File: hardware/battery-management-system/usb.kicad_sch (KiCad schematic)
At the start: 20 parts, among them J12 AMPHENOL_micro_usb_10118194-0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, U5 FT230XS

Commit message: fix design errors
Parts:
- renumbered D17 to D15, D18 to D16, J12 to J11, R17 to R15, R18 to R16, R19 to R17, R20 to R18, R21 to R19, R22 to R20, R23 to R21, R24 to R22

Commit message: fix design errors
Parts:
- renumbered D15 to D13, D16 to D14, J11 to J6
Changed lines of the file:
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@@
   (symbol (lib_id "benediktibk:LED_red_0603") (at 218.44 76.2 90) (unit 1)
     (in_bom yes) (on_board yes) (dnp no) (fields_autoplaced)
-    (property "Reference" "D16" (at 224.79 77.186 90)
+    (property "Reference" "D14" (at 224.79 77.186 90)
       (effects (font (size 1.27 1.27)) (justify right))
     )
@@
       (project "battery-management-system"
         (path "/5272f0ff-3069-41a9-bca2-80beede8b4b2/afdb149d-bd78-484c-a496-c5b66260efca"
-          (reference "D16") (unit 1)
+          (reference "D14") (unit 1)
         )
       )
@@
   (symbol (lib_id "benediktibk:LED_green_0603") (at 201.93 76.2 90) (unit 1)
     (in_bom yes) (on_board yes) (dnp no) (fields_autoplaced)
-    (property "Reference" "D15" (at 208.28 77.7454 90)
+    (property "Reference" "D13" (at 208.28 77.7454 90)
       (effects (font (size 1.27 1.27)) (justify right))
     )
@@
       (project "battery-management-system"
         (path "/5272f0ff-3069-41a9-bca2-80beede8b4b2/afdb149d-bd78-484c-a496-c5b66260efca"
-          (reference "D15") (unit 1)
+          (reference "D13") (unit 1)
         )
       )
@@
   (symbol (lib_id "benediktibk:AMPHENOL_micro_usb_10118194-0001LF") (at 125.73 45.72 0) (unit 1)
     (in_bom yes) (on_board yes) (dnp no) (fields_autoplaced)
-    (property "Reference" "J11" (at 126.619 30.48 0)
+    (property "Reference" "J6" (at 126.619 30.48 0)
       (effects (font (size 1.27 1.27)))
     )
@@
       (project "battery-management-system"
         (path "/5272f0ff-3069-41a9-bca2-80beede8b4b2/afdb149d-bd78-484c-a496-c5b66260efca"
-          (reference "J11") (unit 1)
-        )
-      )
+          (reference "J6") (unit 1)
+        )
+      )

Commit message: add heatsink and fix ERC errors
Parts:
- R21, R22: RS order number 901-3529 -> 199-5452
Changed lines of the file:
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@@
       (effects (font (size 1.27 1.27)) hide)
     )
-    (property "RS order number" "901-3529" (at 200.66 64.77 0)
+    (property "RS order number" "199-5452" (at 200.66 64.77 0)
       (effects (font (size 1.27 1.27)) hide)
     )
@@
       (effects (font (size 1.27 1.27)) hide)
     )
-    (property "RS order number" "901-3529" (at 184.15 64.77 0)
-      (effects (font (size 1.27 1.27)) hide)
-    )
+    (property "RS order number" "199-5452" (at 184.15 64.77 0)
+      (effects (font (size 1.27 1.27)) hide)
+    )

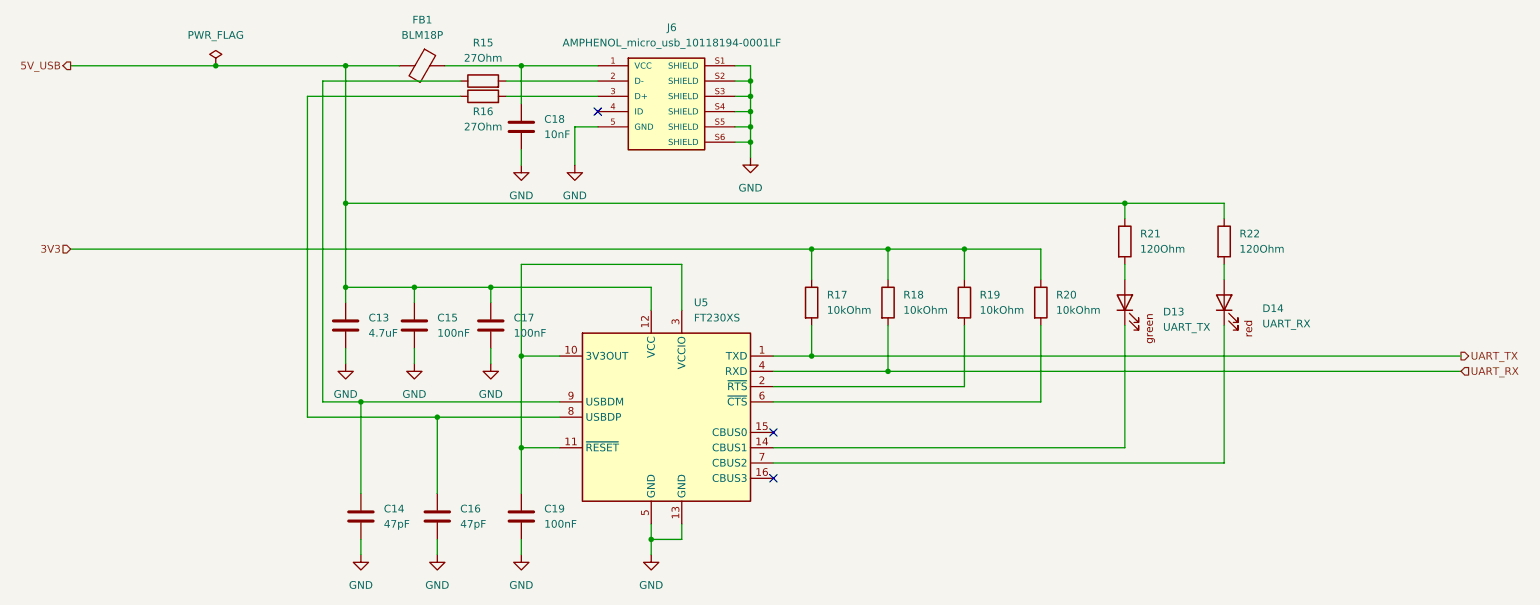
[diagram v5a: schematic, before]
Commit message: add snubber circuit
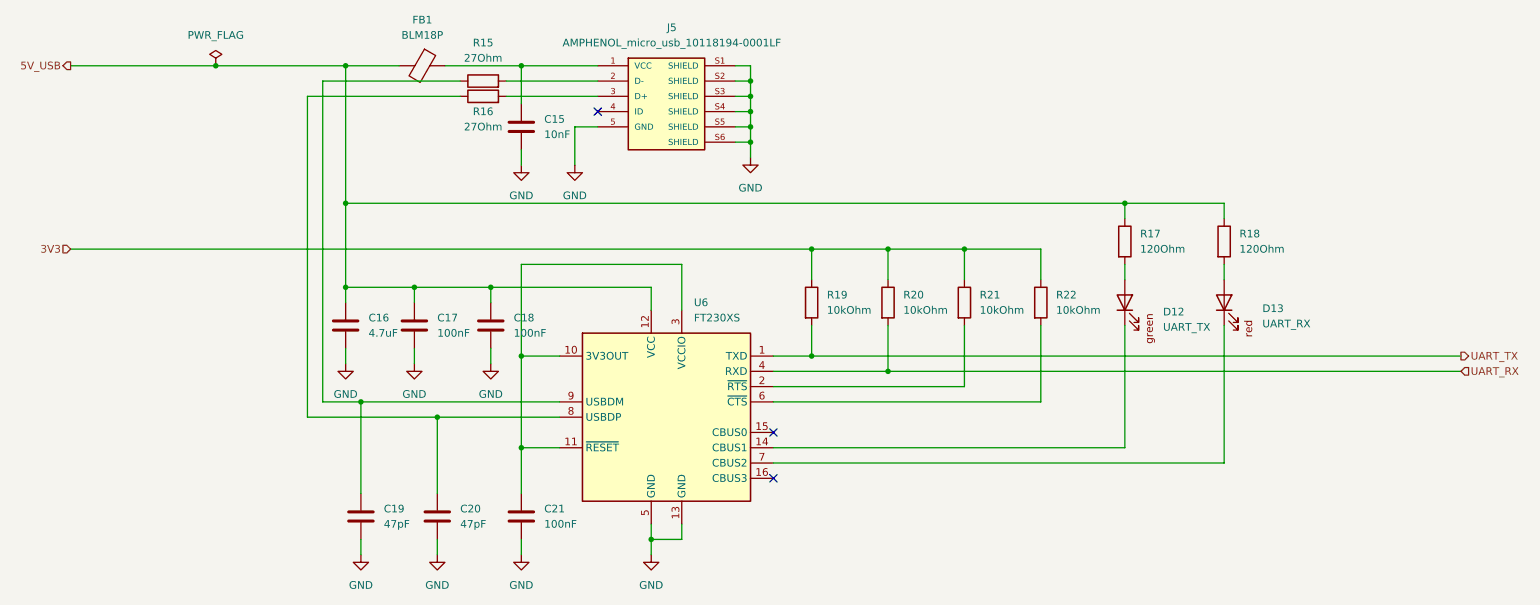
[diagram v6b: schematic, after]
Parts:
- renumbered C18 to C15, C13 to C16, C15 to C17, C17 to C18, C14 to C19, C16 to C20, C19 to C21, D13 to D12, D14 to D13, J6 to J5, R21 to R17, R22 to R18, R17 to R19, R18 to R20, R19 to R21, R20 to R22, U5 to U6
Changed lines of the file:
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@@
 		(dnp no)
 		(fields_autoplaced yes)
-		(property "Reference" "R17"
+		(property "Reference" "R19"
 			(at 152.4 74.9299 0)
 			(effects
@@
 			(project "battery-management-system"
 				(path "/5272f0ff-3069-41a9-bca2-80beede8b4b2/afdb149d-bd78-484c-a496-c5b66260efca"
-					(reference "R17")
+					(reference "R19")
 					(unit 1)
 				)
@@
 		(dnp no)
 		(fields_autoplaced yes)
-		(property "Reference" "U5"
+		(property "Reference" "U6"
 			(at 130.2894 76.2 0)
 			(effects
@@
 			(project "battery-management-system"
 				(path "/5272f0ff-3069-41a9-bca2-80beede8b4b2/afdb149d-bd78-484c-a496-c5b66260efca"
-					(reference "U5")
+					(reference "U6")
 					(unit 1)
 				)
@@
 		(dnp no)
 		(fields_autoplaced yes)
-		(property "Reference" "C19"
+		(property "Reference" "C21"
 			(at 105.41 110.4899 0)
 			(effects
@@
 			(project "battery-management-system"
 				(path "/5272f0ff-3069-41a9-bca2-80beede8b4b2/afdb149d-bd78-484c-a496-c5b66260efca"
-					(reference "C19")
+					(reference "C21")
 					(unit 1)
 				)
@@
 		(dnp no)
 		(fields_autoplaced yes)
-		(property "Reference" "#PWR035"
+		(property "Reference" "#PWR043"
 			(at 87.63 124.46 0)
 			(effects
@@
 			(project "battery-management-system"
 				(path "/5272f0ff-3069-41a9-bca2-80beede8b4b2/afdb149d-bd78-484c-a496-c5b66260efca"
-					(reference "#PWR035")
+					(reference "#PWR043")
 					(unit 1)
 				)
@@
 		(dnp no)
 		(fields_autoplaced yes)
-		(property "Reference" "#PWR034"
+		(property "Reference" "#PWR040"
 			(at 83.82 92.71 0)
 			(effects
@@
 			(project "battery-management-system"
 				(path "/5272f0ff-3069-41a9-bca2-80beede8b4b2/afdb149d-bd78-484c-a496-c5b66260efca"
-					(reference "#PWR034")
+					(reference "#PWR040")
 					(unit 1)
 				)
@@
 		(dnp no)
 		(fields_autoplaced yes)
-		(property "Reference" "D14"
+		(property "Reference" "D13"
 			(at 224.79 77.186 90)
 			(effects
@@
 			(project "battery-management-system"
 				(path "/5272f0ff-3069-41a9-bca2-80beede8b4b2/afdb149d-bd78-484c-a496-c5b66260efca"
-					(reference "D14")
+					(reference "D13")
 					(unit 1)
 				)
@@
 		(dnp no)
 		(fields_autoplaced yes)
-		(property "Reference" "C13"
+		(property "Reference" "C16"
 			(at 76.2 78.7399 0)
 			(effects
@@
 			(project "battery-management-system"
 				(path "/5272f0ff-3069-41a9-bca2-80beede8b4b2/afdb149d-bd78-484c-a496-c5b66260efca"
-					(reference "C13")
+					(reference "C16")
 					(unit 1)
 				)
@@
 		(dnp no)
 		(fields_autoplaced yes)
-		(property "Reference" "C18"
+		(property "Reference" "C15"
 			(at 105.41 45.7199 0)
 			(effects
@@
 			(project "battery-management-system"
 				(path "/5272f0ff-3069-41a9-bca2-80beede8b4b2/afdb149d-bd78-484c-a496-c5b66260efca"
-					(reference "C18")
+					(reference "C15")
 					(unit 1)
 				)
@@
 		(dnp no)
 		(fields_autoplaced yes)
-		(property "Reference" "C17"
+		(property "Reference" "C18"
 			(at 100.33 78.7399 0)
 			(effects
@@
 			(project "battery-management-system"
 				(path "/5272f0ff-3069-41a9-bca2-80beede8b4b2/afdb149d-bd78-484c-a496-c5b66260efca"
-					(reference "C17")
+					(reference "C18")
 					(unit 1)
 				)
@@
 		(dnp no)
 		(fields_autoplaced yes)
-		(property "Reference" "#PWR041"
+		(property "Reference" "#PWR036"
 			(at 139.7 58.42 0)
 			(effects
@@
 			(project "battery-management-system"
 				(path "/5272f0ff-3069-41a9-bca2-80beede8b4b2/afdb149d-bd78-484c-a496-c5b66260efca"
-					(reference "#PWR041")
+					(reference "#PWR036")
 					(unit 1)
 				)
@@
 		(dnp no)
 		(fields_autoplaced yes)
-		(property "Reference" "C15"
+		(property "Reference" "C17"
 			(at 87.63 78.7399 0)
 			(effects
@@
 			(project "battery-management-system"
 				(path "/5272f0ff-3069-41a9-bca2-80beede8b4b2/afdb149d-bd78-484c-a496-c5b66260efca"
-					(reference "C15")
+					(reference "C17")
 					(unit 1)
 				)
@@
 		(dnp no)
 		(fields_autoplaced yes)
-		(property "Reference" "#PWR033"
+		(property "Reference" "#PWR042"
 			(at 74.93 124.46 0)
 			(effects
@@
 			(project "battery-management-system"
 				(path "/5272f0ff-3069-41a9-bca2-80beede8b4b2/afdb149d-bd78-484c-a496-c5b66260efca"
-					(reference "#PWR033")
+					(reference "#PWR042")
 					(unit 1)
 				)
@@
 		(dnp no)
 		(fields_autoplaced yes)
-		(property "Reference" "R22"
+		(property "Reference" "R18"
 			(at 220.98 64.7699 0)
 			(effects
@@
 			(project "battery-management-system"
 				(path "/5272f0ff-3069-41a9-bca2-80beede8b4b2/afdb149d-bd78-484c-a496-c5b66260efca"
-					(reference "R22")
+					(reference "R18")
 					(unit 1)
 				)
@@
 		(dnp no)
 		(fields_autoplaced yes)
-		(property "Reference" "#PWR036"
+		(property "Reference" "#PWR041"
 			(at 96.52 92.71 0)
 			(effects
@@
 			(project "battery-management-system"
 				(path "/5272f0ff-3069-41a9-bca2-80beede8b4b2/afdb149d-bd78-484c-a496-c5b66260efca"
-					(reference "#PWR036")
+					(reference "#PWR041")
 					(unit 1)
 				)
@@
 		(dnp no)
 		(fields_autoplaced yes)
-		(property "Reference" "R18"
+		(property "Reference" "R20"
 			(at 165.1 74.9299 0)
 			(effects
@@
 			(project "battery-management-system"
 				(path "/5272f0ff-3069-41a9-bca2-80beede8b4b2/afdb149d-bd78-484c-a496-c5b66260efca"
-					(reference "R18")
+					(reference "R20")
 					(unit 1)
 				)
@@
 		(dnp no)
 		(fields_autoplaced yes)
-		(property "Reference" "#PWR032"
+		(property "Reference" "#PWR039"
 			(at 72.39 92.71 0)
 			(effects
@@
 			(project "battery-management-system"
 				(path "/5272f0ff-3069-41a9-bca2-80beede8b4b2/afdb149d-bd78-484c-a496-c5b66260efca"
-					(reference "#PWR032")
+					(reference "#PWR039")
 					(unit 1)
 				)
@@
 		(dnp no)
 		(fields_autoplaced yes)
-		(property "Reference" "R19"
+		(property "Reference" "R21"
 			(at 177.8 74.9299 0)
 			(effects
@@
 			(project "battery-management-system"
 				(path "/5272f0ff-3069-41a9-bca2-80beede8b4b2/afdb149d-bd78-484c-a496-c5b66260efca"
-					(reference "R19")
+					(reference "R21")
 					(unit 1)
 				)
@@
 		(dnp no)
 		(fields_autoplaced yes)
-		(property "Reference" "R20"
+		(property "Reference" "R22"
 			(at 190.5 74.9299 0)
 			(effects
@@
 			(project "battery-management-system"
 				(path "/5272f0ff-3069-41a9-bca2-80beede8b4b2/afdb149d-bd78-484c-a496-c5b66260efca"
-					(reference "R20")
+					(reference "R22")
 					(unit 1)
 				)
@@
 		(dnp no)
 		(fields_autoplaced yes)
-		(property "Reference" "C14"
+		(property "Reference" "C19"
 			(at 78.74 110.4899 0)
 			(effects
@@
 			(project "battery-management-system"
 				(path "/5272f0ff-3069-41a9-bca2-80beede8b4b2/afdb149d-bd78-484c-a496-c5b66260efca"
-					(reference "C14")
+					(reference "C19")
 					(unit 1)
 				)
@@
 		(dnp no)
 		(fields_autoplaced yes)
-		(property "Reference" "C16"
+		(property "Reference" "C20"
 			(at 91.44 110.4899 0)
 			(effects
@@
 			(project "battery-management-system"
 				(path "/5272f0ff-3069-41a9-bca2-80beede8b4b2/afdb149d-bd78-484c-a496-c5b66260efca"
-					(reference "C16")
+					(reference "C20")
 					(unit 1)
 				)
@@
 		(dnp no)
 		(fields_autoplaced yes)
-		(property "Reference" "#PWR040"
+		(property "Reference" "#PWR045"
 			(at 123.19 124.46 0)
 			(effects
@@
 			(project "battery-management-system"
 				(path "/5272f0ff-3069-41a9-bca2-80beede8b4b2/afdb149d-bd78-484c-a496-c5b66260efca"
-					(reference "#PWR040")
+					(reference "#PWR045")
 					(unit 1)
 				)
@@
 		(dnp no)
 		(fields_autoplaced yes)
-		(property "Reference" "D13"
+		(property "Reference" "D12"
 			(at 208.28 77.7454 90)
 			(effects
@@
 			(project "battery-management-system"
 				(path "/5272f0ff-3069-41a9-bca2-80beede8b4b2/afdb149d-bd78-484c-a496-c5b66260efca"
-					(reference "D13")
+					(reference "D12")
 					(unit 1)
 				)
@@
 		(dnp no)
 		(fields_autoplaced yes)
-		(property "Reference" "R21"
+		(property "Reference" "R17"
 			(at 204.47 64.7699 0)
 			(effects
@@
 			(project "battery-management-system"
 				(path "/5272f0ff-3069-41a9-bca2-80beede8b4b2/afdb149d-bd78-484c-a496-c5b66260efca"
-					(reference "R21")
+					(reference "R17")
 					(unit 1)
 				)
@@
 		(dnp no)
 		(fields_autoplaced yes)
-		(property "Reference" "#PWR038"
+		(property "Reference" "#PWR044"
 			(at 101.6 124.46 0)
 			(effects
@@
 			(project "battery-management-system"
 				(path "/5272f0ff-3069-41a9-bca2-80beede8b4b2/afdb149d-bd78-484c-a496-c5b66260efca"
-					(reference "#PWR038")
+					(reference "#PWR044")
 					(unit 1)
 				)
@@
 		(dnp no)
 		(fields_autoplaced yes)
-		(property "Reference" "J6"
+		(property "Reference" "J5"
 			(at 126.619 30.48 0)
 			(effects
@@
 			(project "battery-management-system"
 				(path "/5272f0ff-3069-41a9-bca2-80beede8b4b2/afdb149d-bd78-484c-a496-c5b66260efca"
-					(reference "J6")
+					(reference "J5")
 					(unit 1)
 				)
@@
 		(dnp no)
 		(fields_autoplaced yes)
-		(property "Reference" "#PWR039"
+		(property "Reference" "#PWR038"
 			(at 110.49 59.69 0)
 			(effects
@@
 			(project "battery-management-system"
 				(path "/5272f0ff-3069-41a9-bca2-80beede8b4b2/afdb149d-bd78-484c-a496-c5b66260efca"
-					(reference "#PWR039")
-					(unit 1)
-				)
+					(reference "#PWR038")
+					(unit 1)
+				)

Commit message: update symbols from library
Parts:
- C15: Mouser Part Number (none) -> 80-C0603C103M5R3121
- C17, C18, C21: Mouser Part Number (none) -> 581-KGM15BR71H104KM
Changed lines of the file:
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@@
+			)
+		)
+		(property "Mouser Part Number" "581-KGM15BR71H104KM"
+			(at 119.126 110.49 0)
+			(effects
+				(font
+					(size 1.27 1.27)
+				)
+				(hide yes)
 			)
 		)
@@
 			)
 		)
+		(property "Mouser Part Number" "80-C0603C103M5R3121"
+			(at 119.126 45.72 0)
+			(effects
+				(font
+					(size 1.27 1.27)
+				)
+				(hide yes)
+			)
+		)
 		(pin "1"
 		)
@@
 			)
 		)
+		(property "Mouser Part Number" "581-KGM15BR71H104KM"
+			(at 114.046 78.74 0)
+			(effects
+				(font
+					(size 1.27 1.27)
+				)
+				(hide yes)
+			)
+		)
 		(pin "1"
 		)
@@
 			(at 101.346 78.74 0)
 			(effects
+				(font
+					(size 1.27 1.27)
+				)
+				(hide yes)
+			)
+		)
+		(property "Mouser Part Number" "581-KGM15BR71H104KM"
+			(at 101.346 78.74 0)
+			(effects
